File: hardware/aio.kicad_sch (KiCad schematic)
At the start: 0 parts

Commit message: 4-20mA start and PWM as DAC
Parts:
- added C2: C, symbol Device:C
- added C3: 10nF, symbol Device:C
- added Q1: FCX690BTA, EasyEDA:SOT-89-3_L4.5-W2.5-P1.50-LS4.2-BR, symbol EasyEDA:FCX690BTA
- added R1: R, symbol Device:R
- added U1: XTR117AIDGKR, EasyEDA:VSSOP-8_L3.0-W3.0-P0.65-LS5.0-BL, symbol EasyEDA:XTR117AIDGKR
- added U2: ISO7021DR, EasyEDA:SOIC-8_L4.9-W3.9-P1.27-LS6.0-BL, symbol EasyEDA:ISO7021DR
- added U3: OPA333AIDBVR, EasyEDA:SOT-23-5_L3.0-W1.7-P0.95-LS2.8-BR, symbol EasyEDA:OPA333AIDBVR
- added U4: TPS78233DDCR, EasyEDA:SOT-23-5_L3.0-W1.7-P0.95-LS2.8-BR, symbol EasyEDA:TPS78233DDCR
- added U5: INA219AIDCNR, EasyEDA:SOT-23-8_L3.0-W1.7-P0.65-LS2.8-BR, symbol EasyEDA:INA219AIDCNR
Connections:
- new net: U1.2 (IIN), U3.1 (OUT)
- new net: C3.2, U1.4 (IO)
- new net: Q1.3 (E), U1.5 (E)
- new net: Q1.1 (B), U1.6 (B)
- new net: C3.1, Q1.2 (C), U1.7 (V+)
- new net: C2.1, R1.2, U3.4 (IN-)
- new net: R1.1, U2.6 (OUTB)
- no-connect marks 0 -> 1

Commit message: XTR117 Output
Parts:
- removed U2: ISO7021DR, EasyEDA:SOIC-8_L4.9-W3.9-P1.27-LS6.0-BL, symbol EasyEDA:ISO7021DR
- removed U3: OPA333AIDBVR, EasyEDA:SOT-23-5_L3.0-W1.7-P0.95-LS2.8-BR, symbol EasyEDA:OPA333AIDBVR
- removed U4: TPS78233DDCR, EasyEDA:SOT-23-5_L3.0-W1.7-P0.95-LS2.8-BR, symbol EasyEDA:TPS78233DDCR
- added C1: 10nF, symbol Device:C
- added J1, J2: Conn_01x03_Pin, symbol Connector:Conn_01x03_Pin
- added R2: 125k, symbol Device:R
- added R3: 15k, symbol Device:R
- added R4: 620, symbol Device:R
- added R5: 0.1m, symbol Device:R
- added R6: 250, symbol Device:R
- added U2: ISO7041FDBQR, EasyEDA:SSOP-16_L4.9-W3.9-P0.64-LS6.0-BL, symbol EasyEDA:ISO7041FDBQR
- added U4: DAC60501MDGSR, EasyEDA:VSSOP-10_L3.0-W3.0-P0.50-LS4.9-BL, symbol EasyEDA:DAC60501MDGSR
- C2: value C -> 10nF
- R1: value R -> 10k
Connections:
- net at U1.2 (IIN): now also R2.1, R4.2
- net GND_XTR: now reaches U1.3 (IRET)
- net GND_XTR: now also C2.2, R1.2, U2.10 (EN2), U2.9 (GND2), U4.4 (AGND)
- net AO_4-20mA_OUT: now reaches C3.2, U1.4 (IO)
- net AO_4-20mA_IN: now reaches C3.1, Q1.2 (C), U1.7 (V+)
- net 5V_XTR: now reaches U1.8 (VREG)
- net 5V_XTR: now also C2.1, R2.2, U2.16 (VCC2), U4.1 (VDD)
- net AI_4-20mA_IN: now reaches U5.1 (IN+)
- net AI_4-20mA_IN: now also R5.2
- net at U5.2 (IN-): now also R5.1, R6.2
- net at U5.7 (A0): now also J2.2 (Pin_2)
- net at U5.8 (A1): now also J1.2 (Pin_2)
- net at R1.1: now also U4.5 (SPI2C)
- new net: R3.1, U4.2 (VOUT)
- new net: U2.14 (OUTA), U4.6 (SCLK/SCL)
- new net: U2.13 (OUTB), U4.7 (~{SYNC}/A0)
- new net: U2.12 (OUTC), U4.8 (SDIN/SDA)
- new net: R3.2, R4.1
- new net +5V_MCU: C1.2, J1.1 (Pin_1), J2.1 (Pin_1), U2.1 (VCC1)
- new net AI_4-20mA_OUT: R6.1
- new net GND_MCU: C1.1, J1.3 (Pin_3), J2.3 (Pin_3), U2.7 (EN1), U2.8 (GND1)
- new net SPI0_CLK: U2.3 (INA)
- new net SPI0_CS: U2.4 (INB)
- new net SPI0_MISO: U2.6 (OUTD)
- new net SPI0_MOSI: U2.5 (INC)
- no-connect marks 1 -> 4
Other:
- note added: "4-20Ma = 100 X 40-200uA 5V / 125k = 40uA 0-2.5V / 15.62k = 0 - 160uA"
- note added: "4-20mA INPUT"
- note added: "4-20mA OUTPUT (XTR117)"
- note added: "I_O = 100 x I_IN"
- note added: "Pull EN to GND to enable refresh"
- note added: "Pull-down for SPI selection Logic 0 = SPI Logic 1 = I2C"
- note added: "R_LOAD is handled on the 4-20mA current loop receiver R_LOAD = (V_LOOP - V_XTR_MIN) / I_MAX R_LOAD = (24V - 7.5) / 0.02A = 825Ω R_LOAD needs to be < 825Ω"
- moved on the sheet: C3, Q1, U1, U5

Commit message: Almost everything
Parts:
- removed J1, J2: Conn_01x03_Pin, symbol Connector:Conn_01x03_Pin
- removed U5: INA219AIDCNR, EasyEDA:SOT-23-8_L3.0-W1.7-P0.65-LS2.8-BR, symbol EasyEDA:INA219AIDCNR
- added C10, C6, C8, C9: 0.1uF, symbol Device:C
- added C4, C5: 10nF, symbol Device:C
- added C7: 47pF, symbol Device:C
- added Q2: NTF2955T1G, EasyEDA:SOT-223-4_L6.5-W3.5-P2.30-LS7.0-BR, symbol EasyEDA:NTF2955T1G
- added Q3: MMBT2907ALT1G, EasyEDA:SOT-23-3_L2.9-W1.3-P1.90-LS2.4-BR, symbol EasyEDA:MMBT2907ALT1G
- added R10, R11: 2k, symbol Device:R
- added R12, R13: 15, symbol Device:R
- added R14, R16, R17, R18, R19, R22, R9: 10k, symbol Device:R
- added R15: 30k, symbol Device:R
- added R20: 100k, symbol Device:R
- added R21: 20k, symbol Device:R
- added R7: 3, symbol Device:R
- added R8: 250, symbol Device:R
- added U10: REF3040AIDBZR, EasyEDA:SOT-23-3_L2.9-W1.6-P1.90-LS2.8-BR, symbol EasyEDA:REF3040AIDBZR
- added U11, U23: KF301-5.0-2P, EasyEDA:CONN-TH_P5.00_KF301-5.0-2P, symbol EasyEDA:KF301-5.0-2P
- added U12, U6: TLV9301IDBVR, EasyEDA:SOT-23-5_L3.0-W1.7-P0.95-LS2.8-BR, symbol EasyEDA:TLV9301IDBVR
- added U28: DAC8551IADGKR, EasyEDA:VSSOP-8_L3.0-W3.0-P0.65-LS5.0-BL, symbol EasyEDA:DAC8551IADGKR
- added U5: XTR111AIDGQR, EasyEDA:MSOP-10_L3.0-W3.0-P0.50-LS5.0-BL-EP, symbol EasyEDA:XTR111AIDGQR
- added U7: INA226AIDGSR, EasyEDA:MSOP-10_L3.0-W3.0-P0.50-LS5.0-BL, symbol EasyEDA:INA226AIDGSR
- added U8, U9: DAC60501MDGSR, EasyEDA:VSSOP-10_L3.0-W3.0-P0.50-LS4.9-BL, symbol EasyEDA:DAC60501MDGSR
- R5: value 0.1m -> 5.6k
- R6: value 250 -> 8.2k
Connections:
- net AI_4-20mA_IN: now also R7.2, U23.2, U7.10 (VIN+); no longer R5.2
- net at R5.1: now also U5.5 (REGF); no longer R6.2
- net AI_4-20mA_OUT renamed GND
- net GND: now also C10.1, C4.1, C5.2, C6.2, C8.1, C9.2, R10.2, R14.2, R16.2, R17.2, R18.2, R22.1, R8.1, R9.2, U10.3 (GND), U12.2 (V-), U5.10 (GND), U5.11 (PAD), U6.2 (V-), U7.1 (A1), U7.2 (A0), U7.7 (GND), U8.4 (AGND), U9.4 (AGND)
- new net: R10.1, U5.7 (SET)
- new net: Q2.1 (G), Q3.1 (B)
- new net: Q3.2 (E), R12.2, U5.2 (IS)
- new net: Q3.3 (C), U5.3 (VG)
- new net: R9.1, U5.9 (OD)
- new net: R7.1, R8.2, U7.8 (VBUS), U7.9 (VIN-)
- new net: R21.2, U12.1 (OUT), U12.4 (-IN)
- new net: C7.2, R14.1, R15.2, U6.4 (-IN)
- new net: R16.1, U8.5 (SPI2C)
- new net: U6.3 (+IN), U8.2 (VOUT)
- new net: R5.2, R6.2, U5.4 (REGS)
- new net: R19.1, U9.7 (~{SYNC}/A0)
- new net: R18.1, U9.5 (SPI2C)
- new net: R11.1, U5.6 (VIN)
- new net: R11.2, U9.2 (VOUT)
- new net: C4.2, Q2.4 (D), R13.1
- new net: Q2.3 (S), R12.1
- new net: R17.1, U8.7 (~{SYNC}/A0)
- new net: C9.1, U10.2 (OUT), U9.10 (VREFIO)
- new net +12V: C6.1, U12.5 (V+), U6.5 (V+)
- new net +24V: U5.1 (VSP)
- new net +5V: C10.2, C5.1, C8.2, R19.2, U10.1 (IN), U7.6 (VS+), U8.1 (VDD), U9.1 (VDD)
- new net ADC0: R21.1, R22.2
- new net AI_0-10V_GND: R20.1, U11.2
- new net AI_0-10V_IN: R20.2, U12.3 (+IN)
- new net AO_0-10V_OUT: C7.1, R15.1, U11.1, U6.1 (OUT)
- new net AO_4-20mA_SIGNAL: R13.2, U23.1
- new net SCL: U7.5 (SCL), U8.6 (SCLK/SCL), U9.6 (SCLK/SCL)
- new net SDA: U7.4 (SDA), U8.8 (SDIN/SDA), U9.8 (SDIN/SDA)
- no-connect marks 4 -> 12
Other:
- note added: "0-10V INPUT"
- note added: "0-10V OUTPUT"
- note added: "0-2.5V => OP AMP WITH GAIN 4X GAIN = 1 + R_F / R_IN GAIN = 1 + 30/10 = 4"
- note added: "4-20mA OUTPUT (XTR111 )"
- note added: "LOW IMPEDANCE (NEEDS 100K RESISTOR AT RECEIVER)"
- note added: "TERMINALS"
- moved on the sheet: C1, C2, C3, Q1, R1, R2, R3, R4, U1, U2, U4

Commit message: Board complete
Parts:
- removed C1, C2, C3, C5: 10nF, symbol Device:C
- removed C6, C8: 0.1uF, symbol Device:C
- removed C7: 47pF, symbol Device:C
- removed Q1: FCX690BTA, EasyEDA:SOT-89-3_L4.5-W2.5-P1.50-LS4.2-BR, symbol EasyEDA:FCX690BTA
- removed Q2: NTF2955T1G, EasyEDA:SOT-223-4_L6.5-W3.5-P2.30-LS7.0-BR, symbol EasyEDA:NTF2955T1G
- removed R1, R16, R17, R18, R19: 10k, symbol Device:R
- removed R2: 125k, symbol Device:R
- removed R3: 15k, symbol Device:R
- removed R4: 620, symbol Device:R
- removed R5: 5.6k, symbol Device:R
- removed R6: 8.2k, symbol Device:R
- removed R7: 3, symbol Device:R
- removed U1: XTR117AIDGKR, EasyEDA:VSSOP-8_L3.0-W3.0-P0.65-LS5.0-BL, symbol EasyEDA:XTR117AIDGKR
- removed U10: REF3040AIDBZR, EasyEDA:SOT-23-3_L2.9-W1.6-P1.90-LS2.8-BR, symbol EasyEDA:REF3040AIDBZR
- removed U11, U23: KF301-5.0-2P, EasyEDA:CONN-TH_P5.00_KF301-5.0-2P, symbol EasyEDA:KF301-5.0-2P
- removed U2: ISO7041FDBQR, EasyEDA:SSOP-16_L4.9-W3.9-P0.64-LS6.0-BL, symbol EasyEDA:ISO7041FDBQR
- removed U28: DAC8551IADGKR, EasyEDA:VSSOP-8_L3.0-W3.0-P0.65-LS5.0-BL, symbol EasyEDA:DAC8551IADGKR
- removed U4, U8, U9: DAC60501MDGSR, EasyEDA:VSSOP-10_L3.0-W3.0-P0.50-LS4.9-BL, symbol EasyEDA:DAC60501MDGSR
- removed U7: INA226AIDGSR, EasyEDA:MSOP-10_L3.0-W3.0-P0.50-LS5.0-BL, symbol EasyEDA:INA226AIDGSR
- added C11: 1uF, Capacitor_SMD:C_1206_3216Metric_Pad1.33x1.80mm_HandSolder, symbol Device:C
- added C12: 150nF, Capacitor_SMD:C_1206_3216Metric_Pad1.33x1.80mm_HandSolder, symbol Device:C
- added C13, C14, C19: 0.1uF, Capacitor_SMD:C_1206_3216Metric_Pad1.33x1.80mm_HandSolder, symbol Device:C
- added C15: 470nF, Capacitor_SMD:C_1206_3216Metric_Pad1.33x1.80mm_HandSolder, symbol Device:C
- added C18: 1nF, Capacitor_SMD:C_1206_3216Metric_Pad1.33x1.80mm_HandSolder, symbol Device:C
- added IC1: DAC7562SDGSR, Samacsys:SOP50P490X110-10N, symbol Samacsys:DAC7562SDGSR
- added J10, J11, J12, J9: TB007-508-02BE, Samacsys:TB00750802BE, symbol Samacsys:TB007-508-02BE
- added L3: 4.7uH, Samacsys:INDC3225X120N, symbol Samacsys:LQM31PN4R7M00L
- added L4: 1uH, Samacsys:LQM31PN1R0M00L, symbol Samacsys:LQM31PN1R0M00L
- added Q5: BSP171PH6327XTSA1, EasyEDA:SOT-223-4_L6.5-W3.5-P2.30-LS7.0-BR, symbol EasyEDA:BSP171PH6327XTSA1
- added R29: 22k, Resistor_SMD:R_1206_3216Metric_Pad1.30x1.75mm_HandSolder, symbol Device:R
- added R30: 33k, Resistor_SMD:R_1206_3216Metric_Pad1.30x1.75mm_HandSolder, symbol Device:R
- added TP10: TP_AI_0-10V, TestPoint:TestPoint_THTPad_2.0x2.0mm_Drill1.0mm, symbol Connector:TestPoint
- added TP11: TP_ADC1, TestPoint:TestPoint_THTPad_2.0x2.0mm_Drill1.0mm, symbol Connector:TestPoint
- added TP8: TP_AO_0-10V, TestPoint:TestPoint_THTPad_2.0x2.0mm_Drill1.0mm, symbol Connector:TestPoint
- added TP9: TP_ADC0, TestPoint:TestPoint_THTPad_2.0x2.0mm_Drill1.0mm, symbol Connector:TestPoint
- C10, C9: value 0.1uF -> 10uF; footprint (none) -> Capacitor_SMD:C_1206_3216Metric_Pad1.33x1.80mm_HandSolder
- C16: renamed from C4; footprint (none) -> Capacitor_SMD:C_1206_3216Metric_Pad1.33x1.80mm_HandSolder
- R20: footprint (none) -> Resistor_SMD:R_1206_3216Metric_Pad1.30x1.75mm_HandSolder
- R21: renamed from R14; footprint (none) -> Resistor_SMD:R_1206_3216Metric_Pad1.30x1.75mm_HandSolder
- R22: renamed from R21; value 20k -> 56k; footprint (none) -> Resistor_SMD:R_1206_3216Metric_Pad1.30x1.75mm_HandSolder
- R23: renamed from R22; value 10k -> 24k; footprint (none) -> Resistor_SMD:R_1206_3216Metric_Pad1.30x1.75mm_HandSolder
- R24: renamed from R15; footprint (none) -> Resistor_SMD:R_1206_3216Metric_Pad1.30x1.75mm_HandSolder
- R25: renamed from R10; value 2k -> 1.25k; footprint (none) -> Resistor_SMD:R_1206_3216Metric_Pad1.30x1.75mm_HandSolder
- R26: renamed from R9; footprint (none) -> Resistor_SMD:R_1206_3216Metric_Pad1.30x1.75mm_HandSolder
- R27: renamed from R11; value 2k -> 0R; footprint (none) -> Resistor_SMD:R_1206_3216Metric_Pad1.30x1.75mm_HandSolder
- R28: renamed from R8; value 250 -> 250R; footprint (none) -> Resistor_SMD:R_1206_3216Metric_Pad1.30x1.75mm_HandSolder
- R31: renamed from R12; footprint (none) -> Resistor_SMD:R_1206_3216Metric_Pad1.30x1.75mm_HandSolder
- R32: renamed from R13; footprint (none) -> Resistor_SMD:R_1206_3216Metric_Pad1.30x1.75mm_HandSolder
- renumbered Q3 to Q4, U12 to U13, U6 to U14, U5 to U15
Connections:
- net AI_0-10V_GND is gone; now on net GND: R20.1
- net +12V: now also L4.1; no longer U13.5 (V+), U14.5 (V+)
- net +24V: now also C19.2
- net +5V: now also L3.1; no longer C10.2
- net ADC0: now also TP9.1
- net AI_0-10V_IN: now also J9.1, TP10.1
- net AI_4-20mA_IN: now also R28.2, J11.1, R29.2
- net GND: now also C10.2, C11.1, C12.2, C13.2, C14.2, C15.1, C18.1, C19.1, IC1.3 (GND), IC1.4 (~{LDAC}), J10.2, J11.2, J12.2, J9.2, R30.1; no longer C10.1
- net SPI0_CS: now also IC1.6 (~{SYNC})
- net SPI0_MOSI: now also IC1.8 (DIN)
- net at Q4.1 (B): now also R31.1, Q5.3 (S)
- net at Q4.3 (C), U15.3 (VG): now also Q5.1 (G)
- net DAC_0-10V: now reaches U14.3 (+IN)
- net DAC_0-10V: now also IC1.2 (VOUT_B)
- net at U15.5 (REGF): now also U15.4 (REGS), C15.2
- net DAC_4-20mA: now reaches R27.2
- net DAC_4-20mA: now also IC1.1 (VOUT_A)
- net at C16.2, R32.1: now also Q5.2 (D), Q5.4 (D)
- net at C9.1: now also C11.2, C18.2, IC1.9 (AVDD), L3.2
- net AO_0-10V_OUT renamed AO_0-10V
- net AO_0-10V: now also J10.1, TP8.1
- net AO_4-20mA_SIGNAL renamed AO_4-20mA
- net AO_4-20mA: now also J12.1
- new net: C12.1, IC1.10 (VREFIN/VREFOUT)
- new net +12V_LPF_OP: C10.1, C13.1, C14.1, L4.2, U13.5 (V+), U14.5 (V+)
- new net ADC1: R29.1, R30.2, TP11.1
- new net DAC_RESET: IC1.5 (~{CLR})
- new net SPI0_SCK: IC1.7 (SCLK)
- no-connect marks 12 -> 1
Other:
- note added: "0-2.5V output (internal reference)"
- note added: "5V Buck, f = 1.1MHz => f_cut = 1/10 * f = 110kHz"
- note added: "DAC"
- note added: "I_out = 10 x (V_in / R_set) 20mA = 10 x (2.5 / 1.25k)"
- note added: "V+ for op amps shared by both"
- note added: "V_ADC = (V_1 x R_2) / (R_1 + R_2) example: 10V * 24k / 80k = 3V"
- note removed: "0-2.5V => OP AMP WITH GAIN 4X GAIN = 1 + R_F / R_IN GAIN = 1 + 30/10 = 4"
- note removed: "4-20Ma = 100 X 40-200uA 5V / 125k = 40uA 0-2.5V / 15.62k = 0 - 160uA"
- note removed: "4-20mA OUTPUT (XTR117)"
- note removed: "I_O = 100 x I_IN"
- note removed: "Pull EN to GND to enable refresh"
- note removed: "Pull-down for SPI selection Logic 0 = SPI Logic 1 = I2C"
- note removed: "R_LOAD is handled on the 4-20mA current loop receiver R_LOAD = (V_LOOP - V_XTR_MIN) / I_MAX R_LOAD = (24V - 7.5) / 0.02A = 825Ω R_LOAD needs to be < 825Ω"
- note removed: "TERMINALS"
- moved on the sheet: C16, Q4, R20, R21, R22, R23, R24, R25, R26, R27, R28, R31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

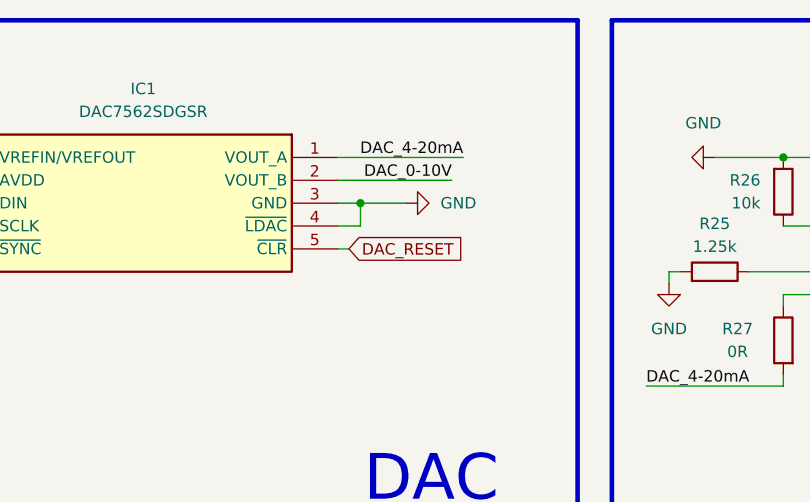
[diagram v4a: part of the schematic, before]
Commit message: LDAC added
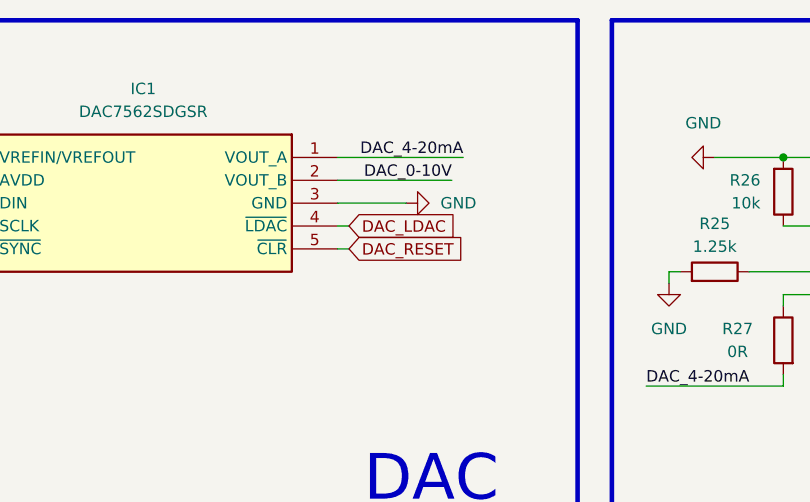
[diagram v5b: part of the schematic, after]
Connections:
- net GND: no longer IC1.4 (~{LDAC})
- new net DAC_LDAC: IC1.4 (~{LDAC})
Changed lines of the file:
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@@
-	)
-	(junction
-		(at 133.35 35.56)
-		(diameter 0)
-		(color 0 0 0 0)
 	)
 	(junction
@@
 	(wire
 		(pts
-			(xy 130.81 35.56) (xy 133.35 35.56)
+			(xy 130.81 35.56) (xy 138.43 35.56)
 		)
 		(stroke
@@
 	(wire
 		(pts
-			(xy 130.81 38.1) (xy 133.35 38.1)
+			(xy 130.81 38.1) (xy 132.08 38.1)
 		)
 		(stroke
@@
 	(wire
 		(pts
-			(xy 133.35 35.56) (xy 138.43 35.56)
-		)
-		(stroke
-			(width 0)
-			(type default)
-		)
-	)
-	(wire
-		(pts
 			(xy 113.03 107.95) (xy 113.03 115.57)
 		)
@@
 		(pts
 			(xy 219.71 187.96) (xy 229.87 187.96)
-		)
-		(stroke
-			(width 0)
-			(type default)
-		)
-	)
-	(wire
-		(pts
-			(xy 133.35 38.1) (xy 133.35 35.56)
 		)
 		(stroke
@@
 			(effects
 				(font
+					(size 1.27 1.27)
+				)
+				(justify left)
+				(hide yes)
+			)
+		)
+	)
+	(global_label "DAC_LDAC"
+		(shape input)
+		(at 132.08 38.1 0)
+		(fields_autoplaced yes)
+		(effects
+			(font
+				(size 1.27 1.27)
+			)
+			(justify left)
+		)
+		(property "Intersheetrefs" "${INTERSHEET_REFS}"
+			(at 144.3181 38.1 0)
+			(effects
+				(font
